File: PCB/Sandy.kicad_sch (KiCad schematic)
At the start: 151 parts, among them J1 USB_C_Receptacle_USB2.0, J16 Conn_01x04, J18 Conn_01x04, J2 Conn_01x03, J3 Conn_01x02, J4 Conn_02x04_Top_Bottom, J5 Conn_02x03_Odd_Even, J6 Conn_02x04_Top_Bottom, J7 Conn_02x04_Top_Bottom, J8 Conn_02x04_Top_Bottom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

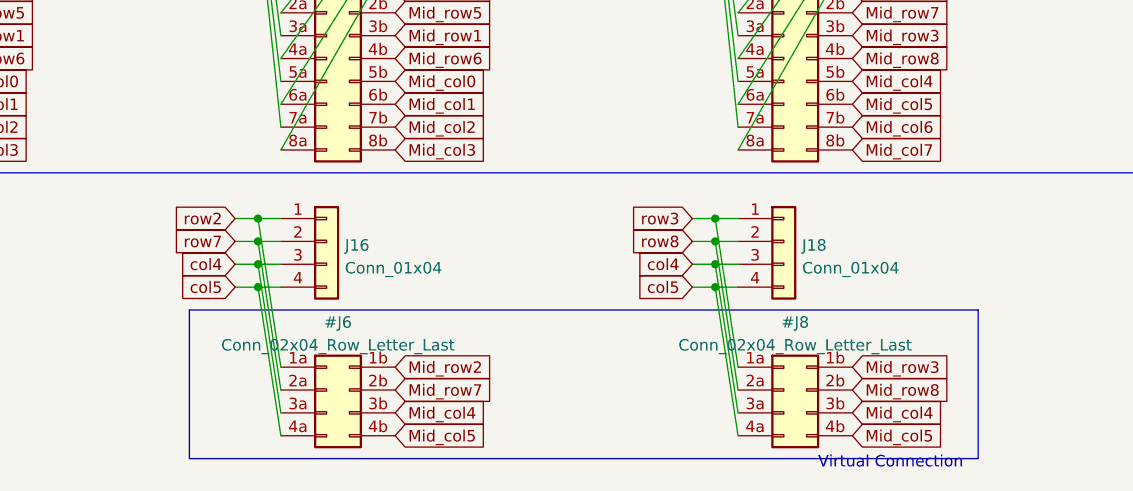
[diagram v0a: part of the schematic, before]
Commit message: 子基板仮配置。コネクタ形状、位置を変更。
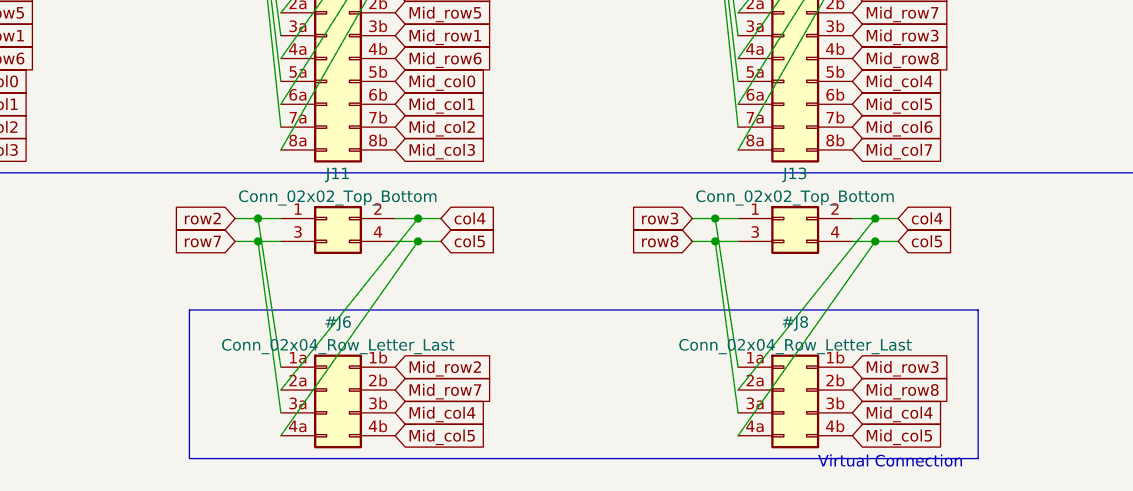
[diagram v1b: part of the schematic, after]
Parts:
- removed J16, J18: Conn_01x04, Connector_PinHeader_2.54mm:PinHeader_1x04_P2.54mm_Vertical, symbol Connector_Generic:Conn_01x04
- added J11, J13: Conn_02x02_Top_Bottom, Connector_PinHeader_2.54mm:PinHeader_2x02_P2.54mm_Vertical, symbol Connector_Generic:Conn_02x02_Odd_Even
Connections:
- net RE_R2_1: now also #J6.2a (Pin_2a), #J8.2a (Pin_2a), J11.2 (Pin_2), J13.2 (Pin_2); no longer #J6.3a (Pin_3a), #J8.3a (Pin_3a)
- net col5: now also J11.4 (Pin_4), J13.4 (Pin_4)
- net row2: now also J11.1 (Pin_1)
- net row3: now also J13.1 (Pin_1)
- net row7: now also #J6.3a (Pin_3a), J11.3 (Pin_3); no longer #J6.2a (Pin_2a)
- net row8: now also #J8.3a (Pin_3a), J13.3 (Pin_3); no longer #J8.2a (Pin_2a)

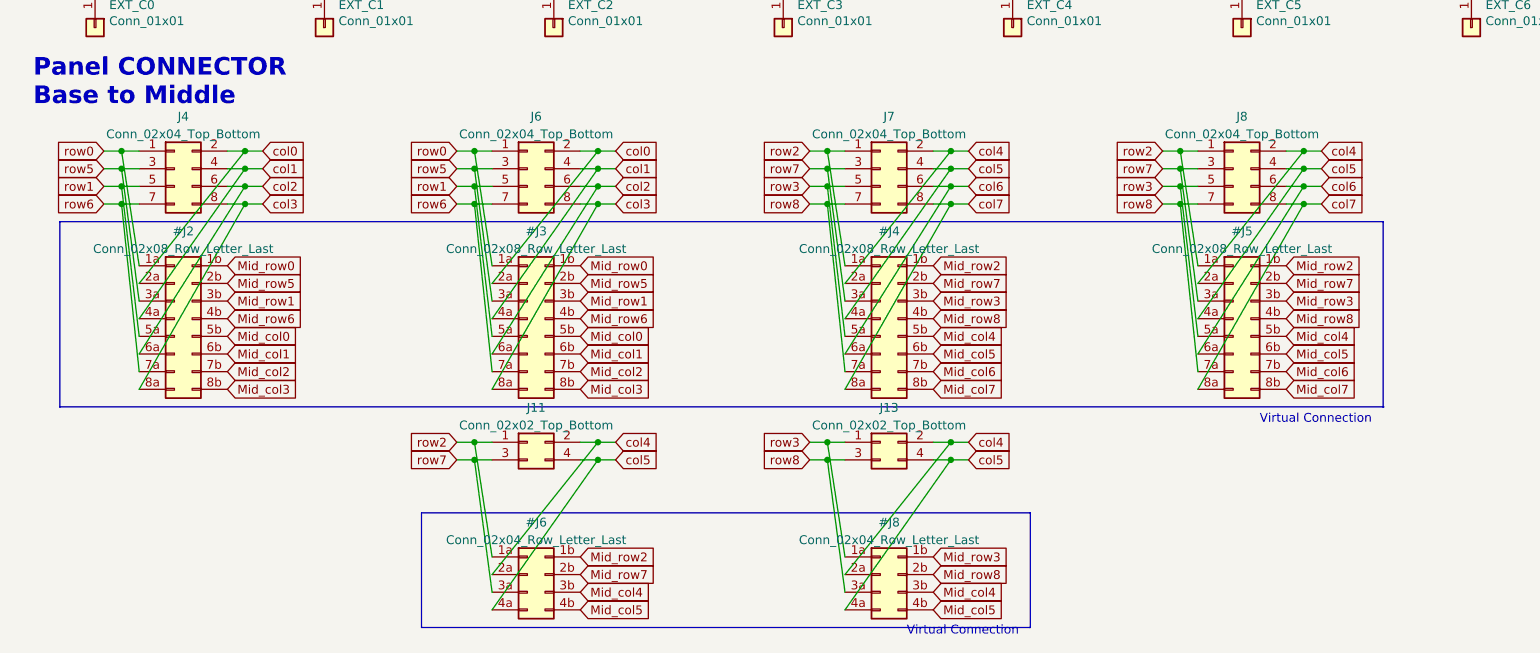
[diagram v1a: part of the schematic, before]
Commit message: 外形、ネジ穴調整
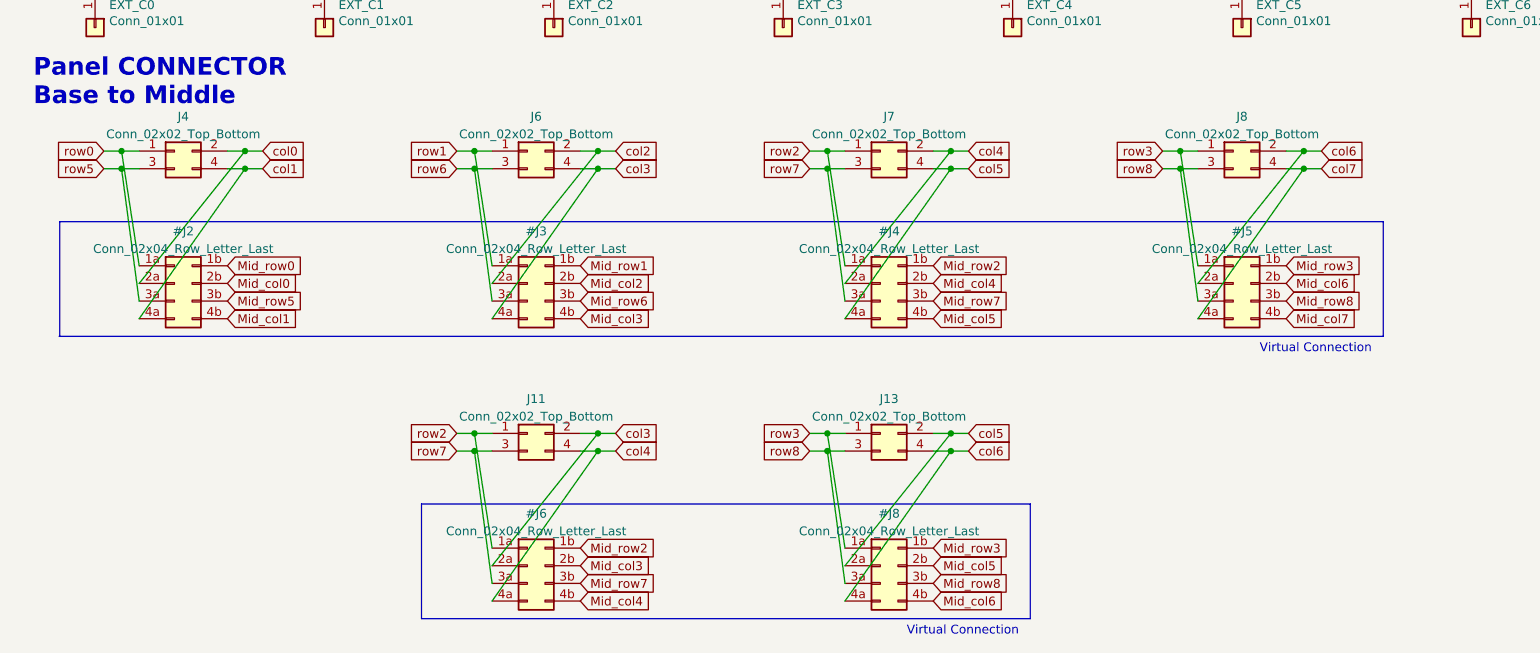
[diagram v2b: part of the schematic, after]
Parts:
- removed #J2, #J3, #J4, #J5: Conn_02x08_Row_Letter_Last, symbol Connector_Generic:Conn_02x08_Row_Letter_Last
- removed J4, J6, J7, J8: Conn_02x04_Top_Bottom, Connector_PinHeader_2.54mm:PinHeader_2x04_P2.54mm_Vertical, symbol Connector_Generic:Conn_02x04_Odd_Even
- added #J2, #J3, #J4, #J5: Conn_02x04_Row_Letter_Last, symbol Connector_Generic:Conn_02x04_Row_Letter_Last
- added J4, J6, J7, J8: Conn_02x02_Top_Bottom, Connector_PinHeader_2.54mm:PinHeader_2x02_P2.54mm_Vertical, symbol Connector_Generic:Conn_02x02_Odd_Even
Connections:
- net MISO: now also #J6.2a (Pin_2a), J11.2 (Pin_2), #J3.4a (Pin_4a), J6.4 (Pin_4)
- net MOSI: now also #J3.2a (Pin_2a), J6.2 (Pin_2)
- net Mid_col0: now also #J2.2b (Pin_2b)
- net Mid_col1: now also #J2.4b (Pin_4b)
- net Mid_col2: now also #J3.2b (Pin_2b)
- net Mid_col3: now also #J6.2b (Pin_2b), #J3.4b (Pin_4b)
- net Mid_col4: now also #J6.4b (Pin_4b), #J4.2b (Pin_2b); no longer #J6.3b (Pin_3b), #J8.3b (Pin_3b)
- net Mid_col5: now also #J8.2b (Pin_2b), #J4.4b (Pin_4b); no longer #J6.4b (Pin_4b), #J8.4b (Pin_4b)
- net Mid_col6: now also #J8.4b (Pin_4b), #J5.2b (Pin_2b)
- net Mid_col7: now also #J5.4b (Pin_4b)
- net Mid_row0: now also #J2.1b (Pin_1b)
- net Mid_row1: now also #J3.1b (Pin_1b)
- net Mid_row2: now also #J4.1b (Pin_1b)
- net Mid_row3: now also #J5.1b (Pin_1b)
- net Mid_row5: now also #J2.3b (Pin_3b)
- net Mid_row6: now also #J3.3b (Pin_3b)
- net Mid_row7: now also #J6.3b (Pin_3b), #J4.3b (Pin_3b); no longer #J6.2b (Pin_2b)
- net Mid_row8: now also #J8.3b (Pin_3b), #J5.3b (Pin_3b); no longer #J8.2b (Pin_2b)
- net RE_L1_1: now also #J2.2a (Pin_2a), J4.2 (Pin_2)
- net RE_R1_1: now also #J5.4a (Pin_4a), J8.4 (Pin_4)
- net RE_R2_1: now also #J6.4a (Pin_4a), J11.4 (Pin_4), #J4.2a (Pin_2a), J7.2 (Pin_2); no longer #J6.2a (Pin_2a), #J8.2a (Pin_2a), J11.2 (Pin_2), J13.2 (Pin_2)
- net SCK: now also #J2.4a (Pin_4a), J4.4 (Pin_4)
- net col5: now also #J8.2a (Pin_2a), J13.2 (Pin_2), #J4.4a (Pin_4a), J7.4 (Pin_4); no longer #J6.4a (Pin_4a), #J8.4a (Pin_4a), J11.4 (Pin_4), J13.4 (Pin_4)
- net col6: now also #J8.4a (Pin_4a), J13.4 (Pin_4), #J5.2a (Pin_2a), J8.2 (Pin_2)
- net row0: now also #J2.1a (Pin_1a), J4.1 (Pin_1)
- net row1: now also #J3.1a (Pin_1a), J6.1 (Pin_1)
- net row2: now also #J4.1a (Pin_1a), J7.1 (Pin_1)
- net row3: now also #J5.1a (Pin_1a), J8.1 (Pin_1)
- net row5: now also #J2.3a (Pin_3a), J4.3 (Pin_3)
- net row6: now also #J3.3a (Pin_3a), J6.3 (Pin_3)
- net row7: now also #J4.3a (Pin_3a), J7.3 (Pin_3)
- net row8: now also #J5.3a (Pin_3a), J8.3 (Pin_3)
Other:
- moved on the sheet: J11, J13

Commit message: キースイッチを配置
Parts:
- J11, J13, J6, J7, J8: footprint Connector_PinHeader_2.54mm:PinHeader_2x02_P2.54mm_Vertical -> Connector_PinHeader_2.00mm:PinHeader_2x02_P2.00mm_Vertical
- J5: renamed from J4; footprint Connector_PinHeader_2.54mm:PinHeader_2x02_P2.54mm_Vertical -> Connector_PinHeader_2.00mm:PinHeader_2x02_P2.00mm_Vertical
- SW_LSFT1.75u1: footprint MX_Alps_Hybrid:MXOnly-1.75U-Hotswap-guide -> MX_Alps_Hybrid:MXOnly-1.75U-NoLED
- SW_LSFT2u1: footprint MX_Alps_Hybrid:MXOnly-2U-Hotswap-ReversedStabilizers-guide -> MX_Alps_Hybrid:MXOnly-2U-Hotswap-guide
- renumbered J5 to J4

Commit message: 部品仮配置
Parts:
- J10: renamed from J13; footprint Connector_PinHeader_2.00mm:PinHeader_2x02_P2.00mm_Vertical -> locallib:PinHeader_2x02_P2.00mm_Vertical_Centered
- J5, J6, J7, J8: footprint Connector_PinHeader_2.00mm:PinHeader_2x02_P2.00mm_Vertical -> locallib:PinHeader_2x02_P2.00mm_Vertical_Centered
- J9: renamed from J11; footprint Connector_PinHeader_2.00mm:PinHeader_2x02_P2.00mm_Vertical -> locallib:PinHeader_2x02_P2.00mm_Vertical_Centered
- SW_CAPS1u1, SW_CenterL1u1, SW_CenterR1u1, SW_RIGHT1: footprint MX_Alps_Hybrid:MXOnly-1U-Hotswap-guide -> MX_Alps_Hybrid:MXOnly-1U-Hotswap-on-RE-guide
- SW_RE_L1, SW_RE_L2, SW_RE_R1, SW_RE_R2: footprint locallib:RotaryEncoder_Alps_EC11K-Switch_Vertical_H20mm -> locallib:RotaryEncoder_Alps_EC11K-Switch_Vertical_H20mm_NPTH_MP

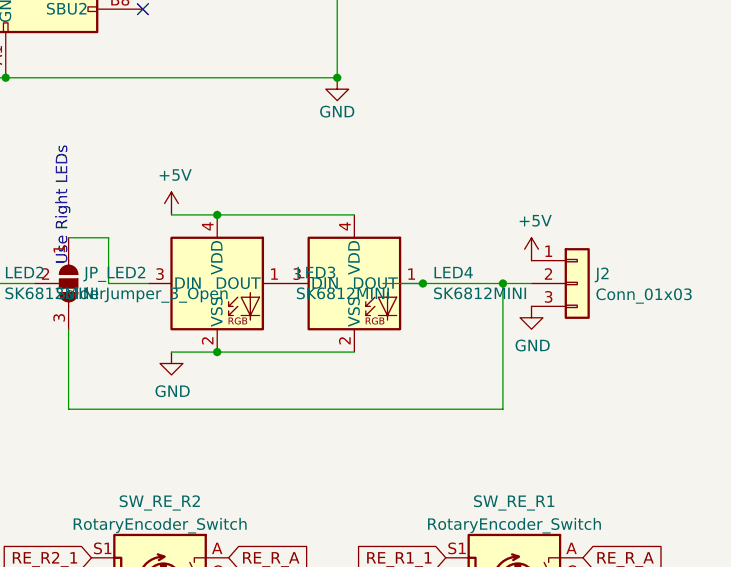
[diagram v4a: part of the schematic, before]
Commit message: スイッチ方向確定。細かな調整
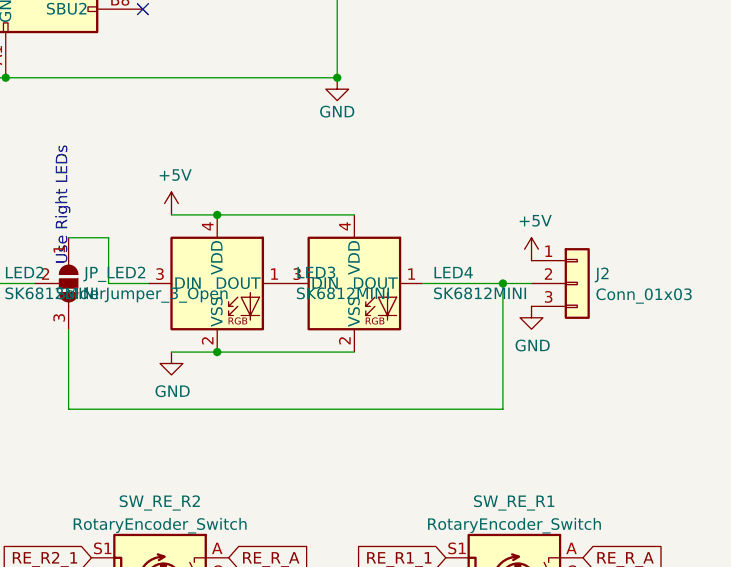
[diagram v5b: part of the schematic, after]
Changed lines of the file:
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@@
   (junction (at 347.345 165.1) (diameter 0) (color 0 0 0 0)
   )
-  (junction (at 376.555 213.36) (diameter 0) (color 0 0 0 0)
-  )
   (junction (at 347.345 170.18) (diameter 0) (color 0 0 0 0)
   )
@@
     (stroke (width 0) (type default) (color 0 0 0 0))
   )
-  (wire (pts (xy 372.11 213.36) (xy 376.555 213.36))
-    (stroke (width 0) (type default) (color 0 0 0 0))
-  )
   (wire (pts (xy 73.66 82.55) (xy 73.66 114.3))
     (stroke (width 0) (type default) (color 0 0 0 0))
@@
       (reference "SW_;2") (unit 1) (value "SW_Push") (footprint "MX_Alps_Hybrid:MXOnly-1U-Hotswap-guide")
     )
-    (path "/657e3a5b-6fed-49ab-8642-9fbc0b768079/5bc38787-012a-4f10-8221-d47e1e812132"
-      (reference "SW_;3") (unit 1) (value "SW_Push") (footprint "MX_Alps_Hybrid:MXOnly-1U-NoLED")
-    )
     (path "/00000000-0000-0000-0000-00005f66ba2b"

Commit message: JSTコネクタとスペーサーでなんとするテスト
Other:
- note added: "Bottom to Mid: require 16 pins"
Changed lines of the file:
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@@
     (effects (font (size 1.27 1.27)) (justify left bottom))
   )
+  (text "Bottom to Mid: require 16 pins" (at 165.1 271.78 0)
+    (effects (font (size 5.08 5.08) (thickness 1.016) bold) (justify left bottom))
+  )
   (text "Panel CONNECTOR\nBase to Middle" (at 15.24 208.28 0)
     (effects (font (size 2.54 2.54) (thickness 0.508) bold) (justify left bottom))
@@
       (reference "D59") (unit 1) (value "D") (footprint "Diode_SMD:D_SOD-123")
     )
+    (path "/657e3a5b-6fed-49ab-8642-9fbc0b768079/73f1126e-ca87-4e09-a1ed-b765b426e7b4"
+      (reference "D60") (unit 1) (value "D") (footprint "Diode_SMD:D_SOD-123")
+    )
+    (path "/657e3a5b-6fed-49ab-8642-9fbc0b768079/ea2e9c6d-5ae0-42fe-a35c-3b7710e3ca82"
+      (reference "D61") (unit 1) (value "D") (footprint "Diode_SMD:D_SOD-123")
+    )
+    (path "/657e3a5b-6fed-49ab-8642-9fbc0b768079/96c16827-6231-4530-b5c3-beed48e5205b"
+      (reference "D62") (unit 1) (value "D") (footprint "Diode_SMD:D_SOD-123")
+    )
+    (path "/657e3a5b-6fed-49ab-8642-9fbc0b768079/74555395-ef4f-4df9-aa65-ba6e2cd5ce99"
+      (reference "D63") (unit 1) (value "D") (footprint "Diode_SMD:D_SOD-123")
+    )
+    (path "/657e3a5b-6fed-49ab-8642-9fbc0b768079/f4f6b2f4-47ed-4341-a133-b7eea3e6b0a6"
+      (reference "D64") (unit 1) (value "D") (footprint "Diode_SMD:D_SOD-123")
+    )
     (path "/00000000-0000-0000-0000-00005f65b38d"
       (reference "D74") (unit 1) (value "D") (footprint "Diode_SMD:D_SOD-123")
@@
     )
     (path "/657e3a5b-6fed-49ab-8642-9fbc0b768079/4e814551-707a-49cd-a5cf-4a7c6dde6d6c"
-      (reference "S?") (unit 1) (value "JS5208") (footprint "SW_JS5208")
+      (reference "S1") (unit 1) (value "JS5208") (footprint "locallib:SW_JS5208_add_MP_hole")
+    )
+    (path "/657e3a5b-6fed-49ab-8642-9fbc0b768079/f19acb18-ba6b-4e84-8e72-30eac013a8b9"
+      (reference "S2") (unit 1) (value "JS5208") (footprint "locallib:SW_JS5208_add_MP_hole")
     )
     (path "/657e3a5b-6fed-49ab-8642-9fbc0b768079/9b60bbe6-6e78-46e7-aacd-e2e4b03eb7ba"

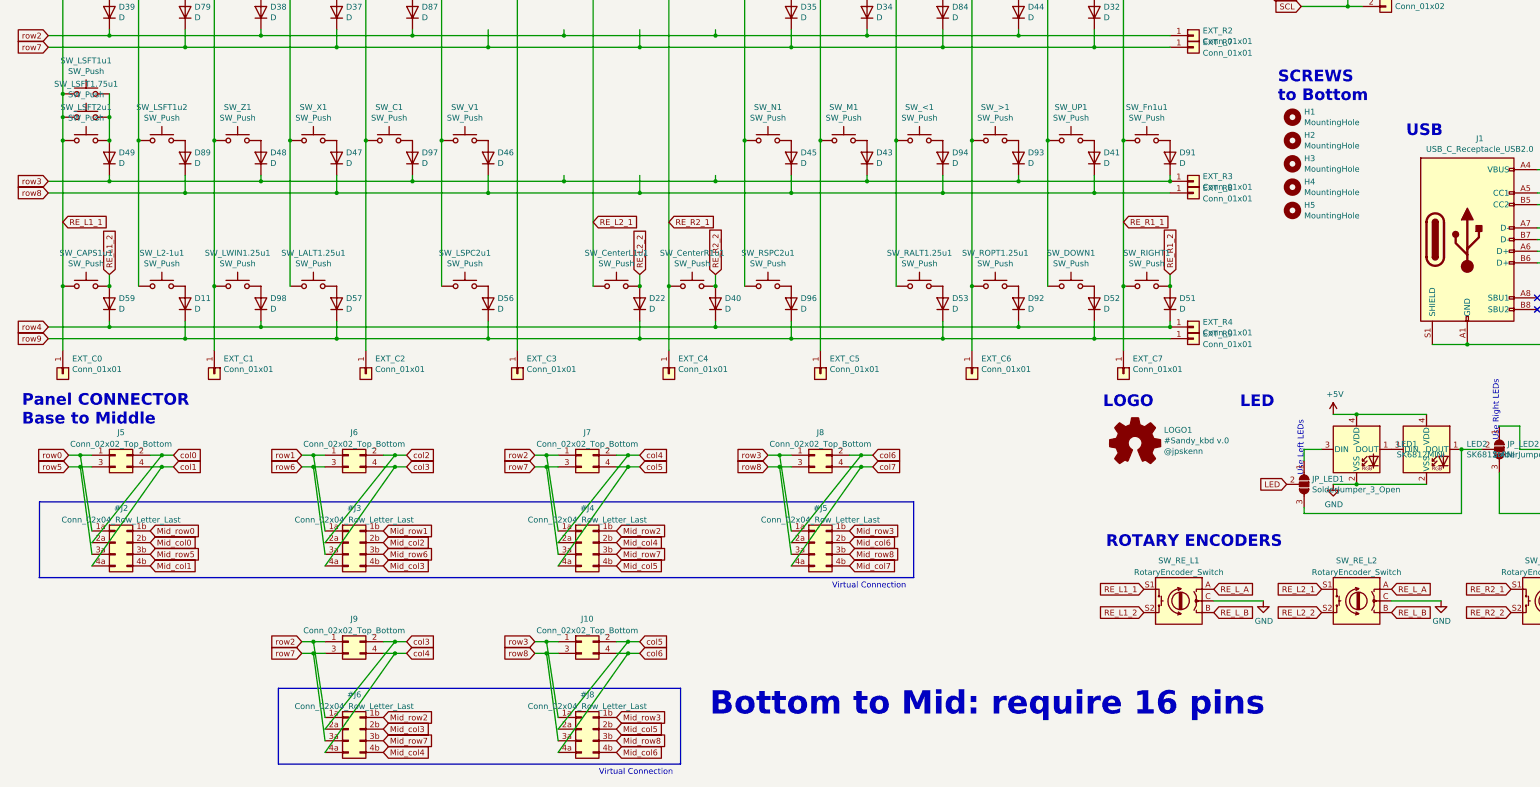
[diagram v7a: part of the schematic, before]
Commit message: JSTコネクタとスペーサーに置き換え
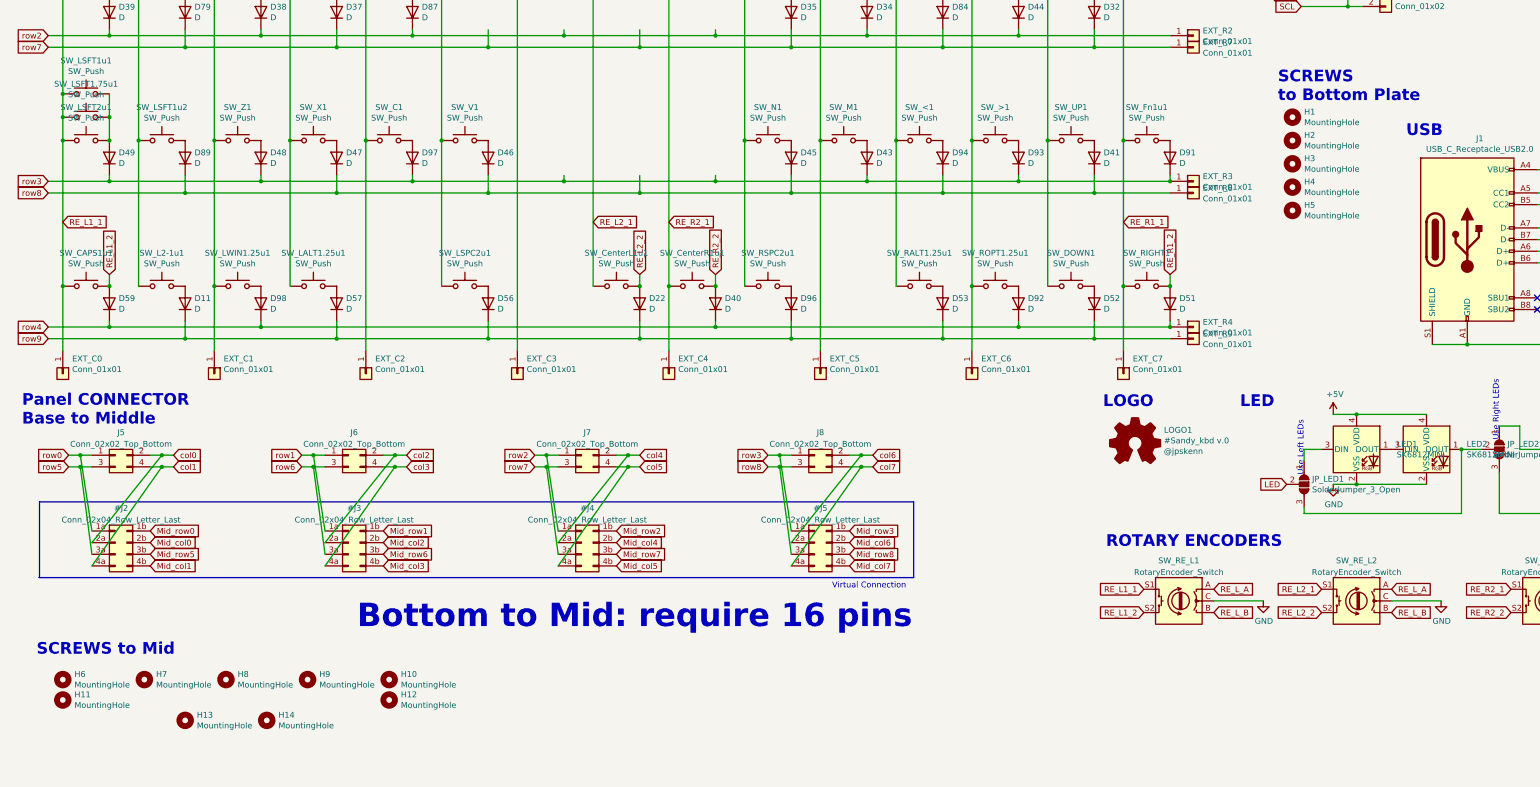
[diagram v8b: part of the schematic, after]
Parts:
- removed #J6, #J8: Conn_02x04_Row_Letter_Last, symbol Connector_Generic:Conn_02x04_Row_Letter_Last
- removed J10, J9: Conn_02x02_Top_Bottom, locallib:PinHeader_2x02_P2.00mm_Vertical_Centered, symbol Connector_Generic:Conn_02x02_Odd_Even
- added H10, H11, H12, H13, H14, H6, H7, H8, H9: MountingHole, MountingHole:MountingHole_2.2mm_M2_No_Cu, symbol Mechanical:MountingHole
- H1, H2, H3, H4, H5: footprint MountingHole:MountingHole_2.2mm_M2 -> MountingHole:MountingHole_2.2mm_M2_No_Cu
- J5, J6, J7, J8: footprint locallib:PinHeader_2x02_P2.00mm_Vertical_Centered -> Connector_JST:JST_SH_SM04B-SRSS-TB_1x04-1MP_P1.00mm_Horizontal
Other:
- note added: "SCREWS to Bottom Plate"
- note added: "SCREWS to Mid"
- note removed: "SCREWS to Bottom"
